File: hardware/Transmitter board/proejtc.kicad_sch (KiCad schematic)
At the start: 8 parts, among them J1 AudioPlug2, U1 LM358

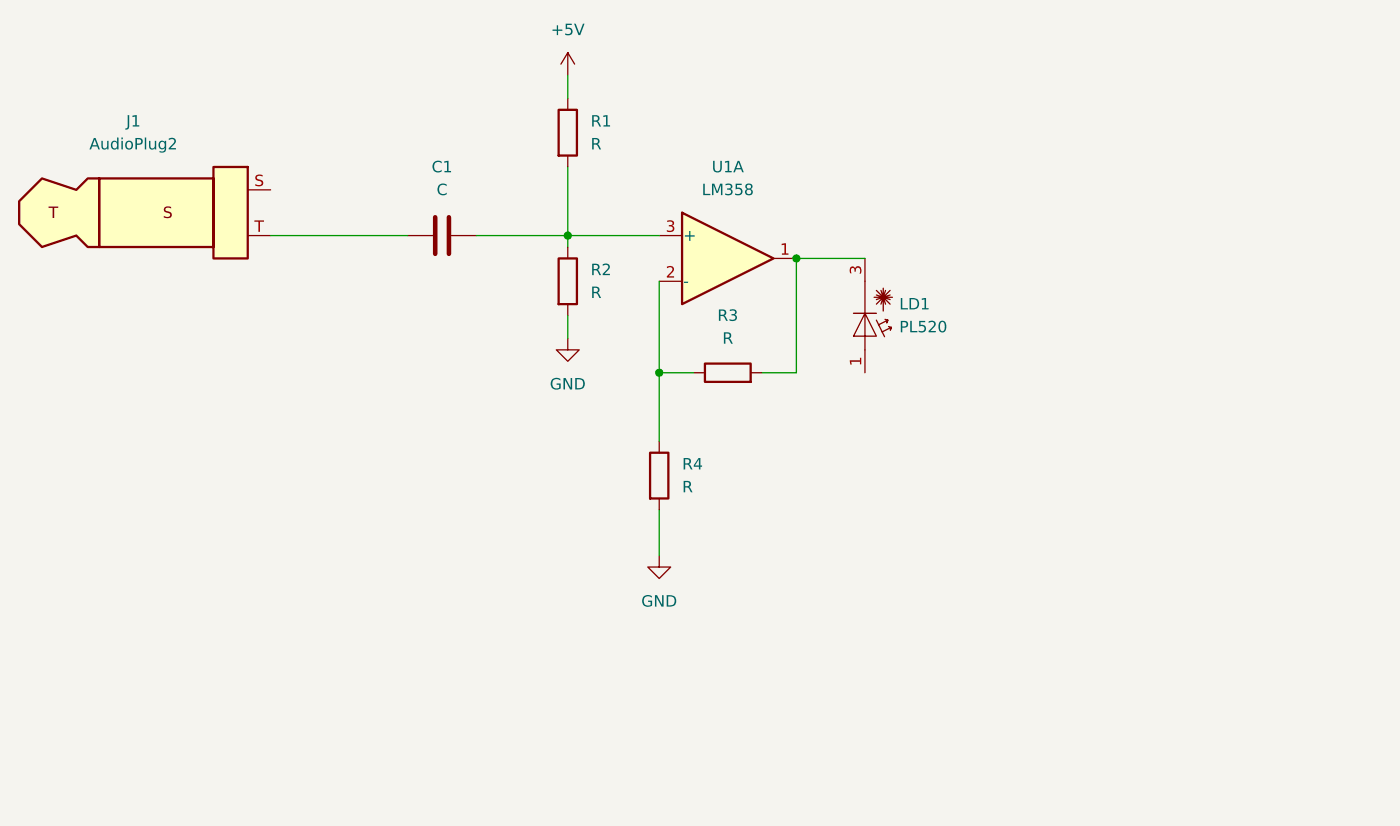
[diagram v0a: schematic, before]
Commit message: Completed the Schematic for Transmitter Board
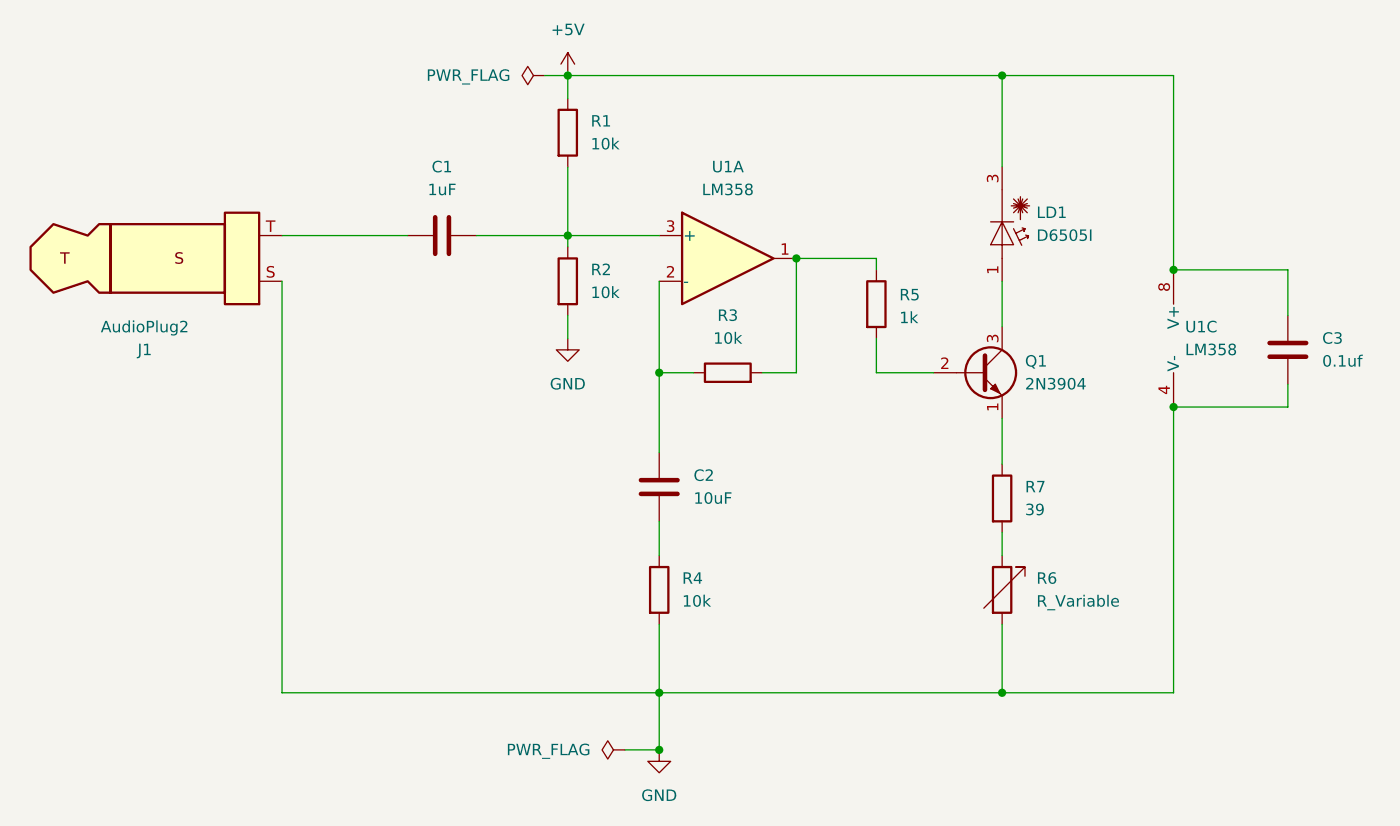
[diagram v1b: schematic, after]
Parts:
- added C2: 10uF, symbol Device:C
- added C3: 0.1uf, symbol Device:C
- added Q1: 2N3904, Package_TO_SOT_THT:TO-92_Inline, symbol Transistor_BJT:2N3904
- added R5: 1k, symbol Device:R
- added R6: R_Variable, symbol Device:R_Variable
- added R7: 39, symbol Device:R
- added unit 3 of U1
- C1: value C -> 1uF
- LD1: value PL520 -> D6505I
- R1, R2, R3, R4: value R -> 10k
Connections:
- net +5V: now also LD1.3 (C), C3.1, U1.8 (V+)
- net GND: now also J1.S, C3.2, R6.2, U1.4 (V-)
- net at R3.1, U1.2 (-): now also C2.1; no longer R4.1
- net at R3.2, U1.1: now also R5.1; no longer LD1.3 (C)
- net at LD1.1 (A): now also Q1.3 (C)
- new net: C2.2, R4.1
- new net: Q1.1 (E), R7.1
- new net: R6.1, R7.2
- new net: Q1.2 (B), R5.2
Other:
- moved on the sheet: J1, LD1, R4
